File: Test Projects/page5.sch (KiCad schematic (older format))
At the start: 29 parts, among them P10 CONN_01X08, P11 CONN_01X08, P2 CONN_01X07, P3 CONN_01X08, P4 CONN_01X08, P5 CONN_01X08, P6 CONN_01X08, P8 CONN_01X08, P9 CONN_01X08, U10 SF-4052, U11 SF-4052, U12 SF-4052, U13 SF-4052, U14 SF-4052, U15 SF-4052, U16 SF-4052, U17 SF-4052, U8 SF-4052, U9 SF-4052

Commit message: Tested a few layout sections
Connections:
- net OUT1 is gone; now on net KOUT1: U8.13 (X)
- net OUT2 is gone; now on net KOUT2: U8.3 (Y)
- net OUT3 is gone; now on net KOUT3: U9.13 (X)
- net OUT4 is gone; now on net KOUT4: U9.3 (Y)
- net OUT5 is gone; now on net KOUT5: U10.13 (X)
- net OUT6 is gone; now on net KOUT6: U10.3 (Y)
- net OUT7 is gone; now on net KOUT7: U11.13 (X)
- net OUT8 is gone; now on net KOUT8: U11.3 (Y)
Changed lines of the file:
@@
 	5700 2950 5650 2950
 Text GLabel 2550 2350 2    50   Input ~ 0
-OUT1
+KOUT1
 Text GLabel 2550 2750 2    50   Input ~ 0
-OUT2
+KOUT2
 Text GLabel 4850 2350 2    50   Input ~ 0
-OUT3
+KOUT3
 Text GLabel 4850 2750 2    50   Input ~ 0
-OUT4
+KOUT4
 Text GLabel 7150 2350 2    50   Input ~ 0
-OUT5
+KOUT5
 Text GLabel 7150 2750 2    50   Input ~ 0
-OUT6
+KOUT6
 Text GLabel 9450 2750 2    50   Input ~ 0
-OUT8
+KOUT8
 Text GLabel 9450 2350 2    50   Input ~ 0
-OUT7
+KOUT7
 Text GLabel 3050 6050 2    50   Input ~ 0
 KA0

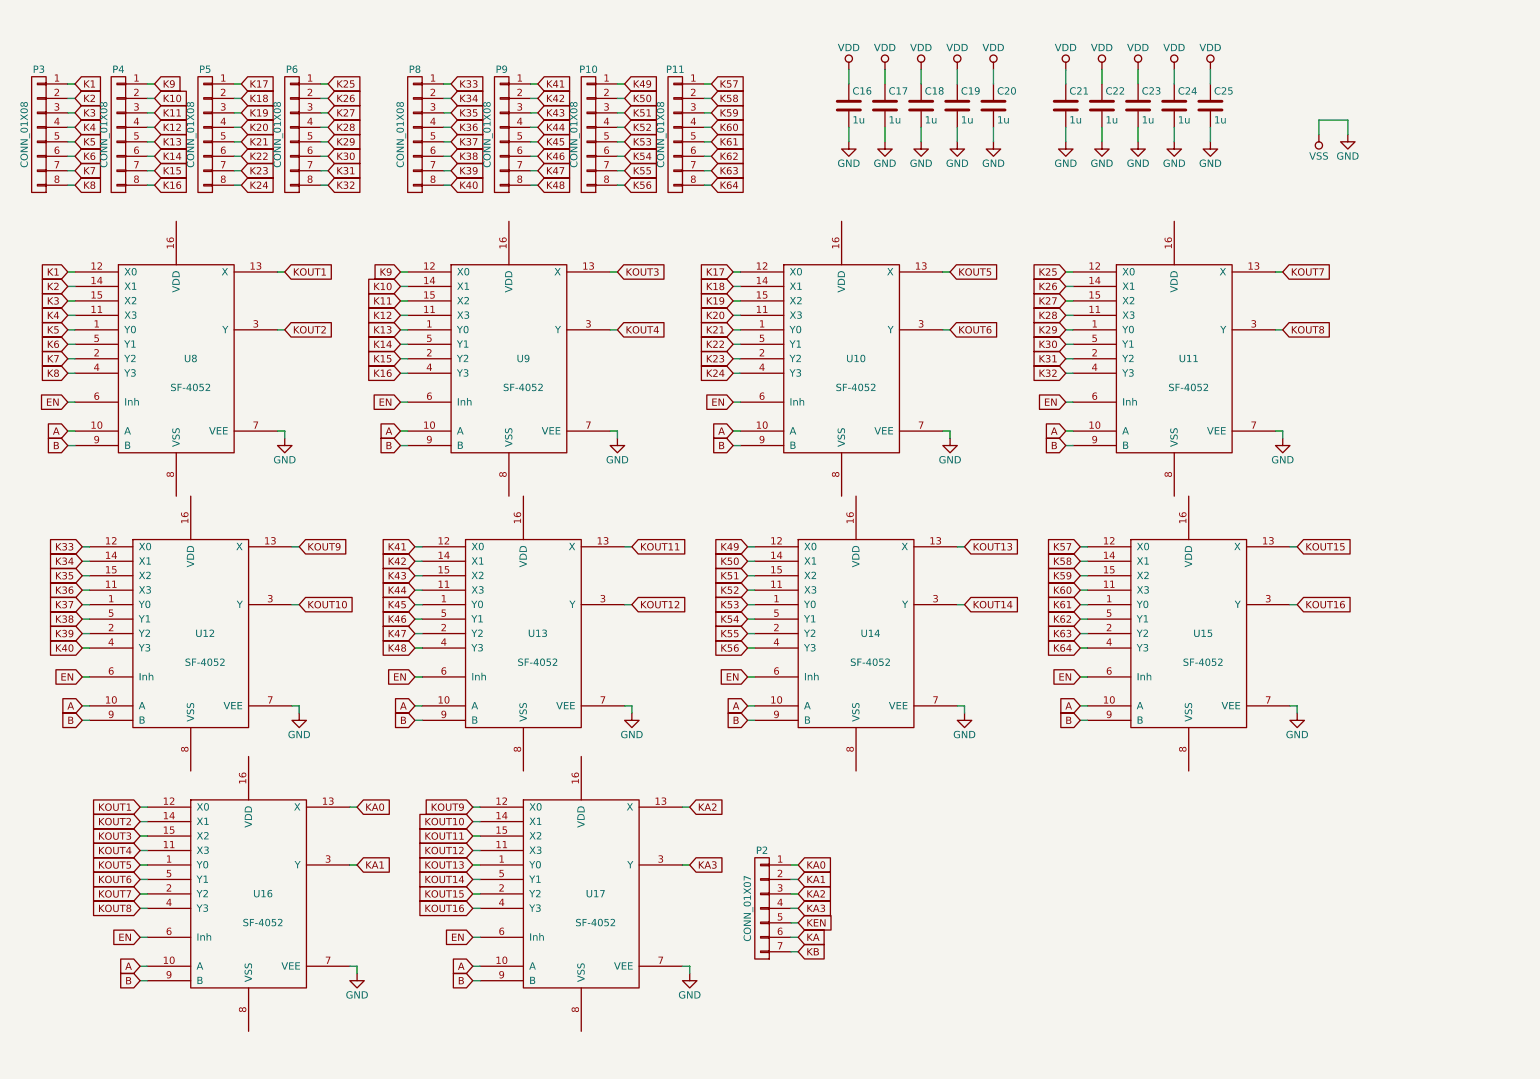
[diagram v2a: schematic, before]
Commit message: Moved to 10x5 size
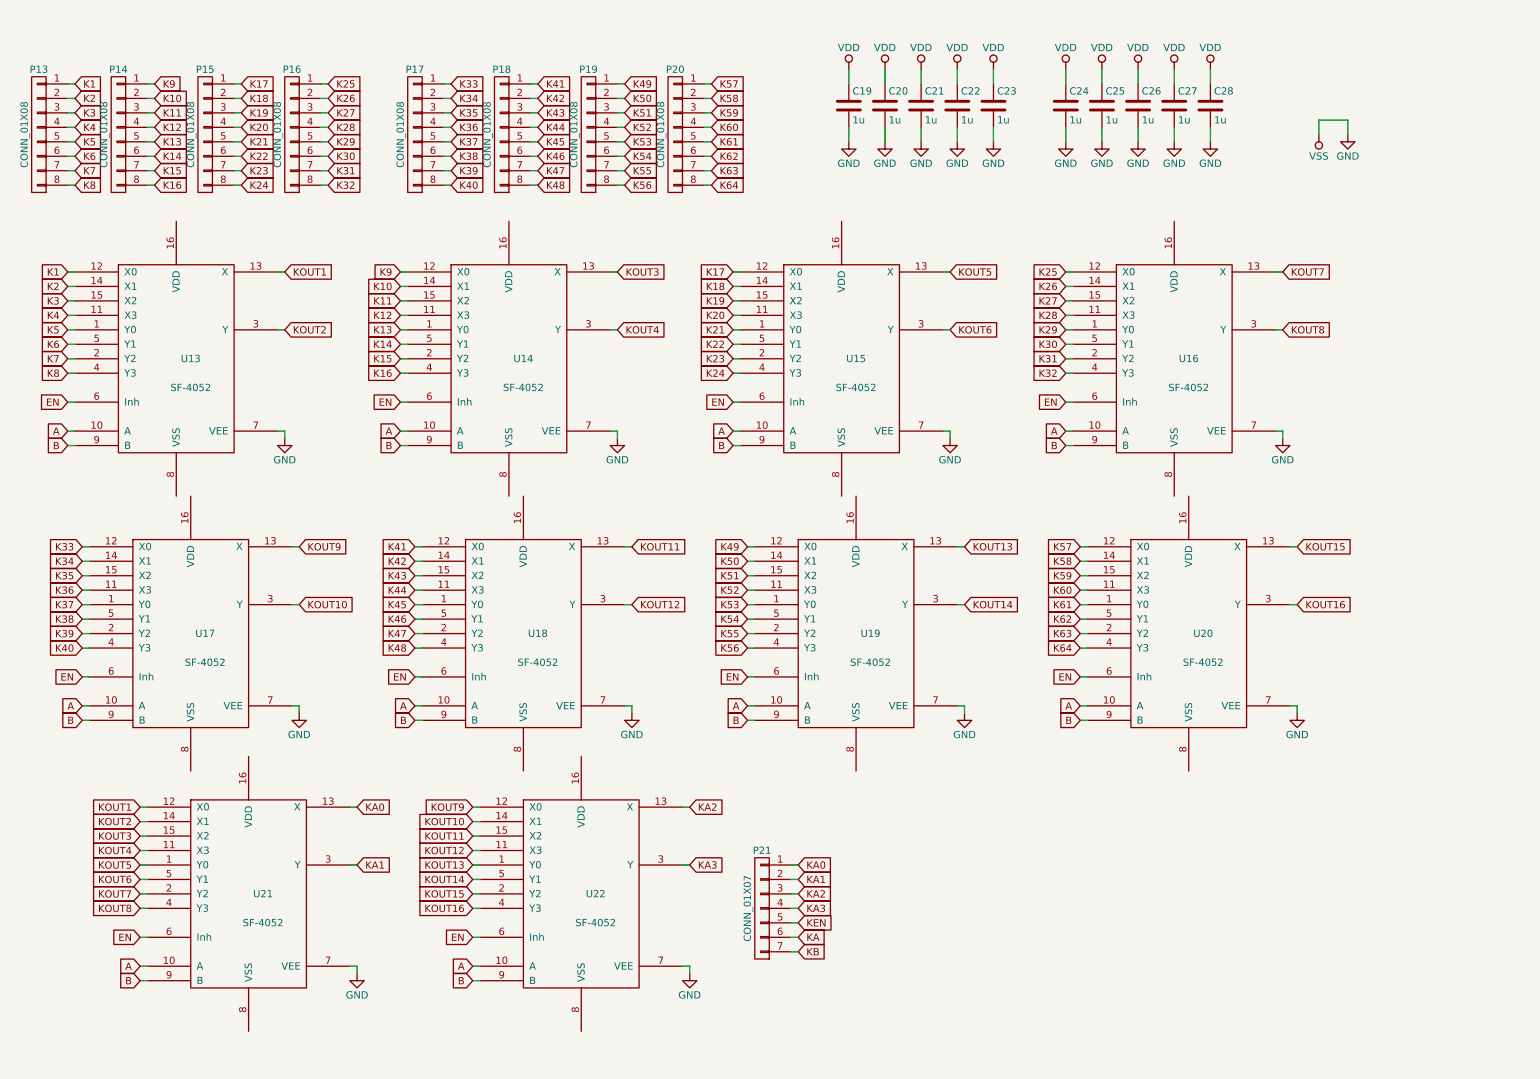
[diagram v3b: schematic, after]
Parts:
- renumbered C16 to C19, C17 to C20, C18 to C21, C19 to C22, C20 to C23, C21 to C24, C22 to C25, C23 to C26, C24 to C27, C25 to C28, P3 to P13, P4 to P14, P5 to P15, P6 to P16, P8 to P17, P9 to P18, P10 to P19, P11 to P20, P2 to P21, U8 to U13, U9 to U14, U10 to U15, U11 to U16, U12 to U17, U13 to U18, U14 to U19, U15 to U20, U16 to U21, U17 to U22
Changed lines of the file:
@@
 $EndDescr
 $Comp
-L C C16
+L C C19
 U 1 1 5688BB67
 P 6450 1200
-F 0 "C16" H 6475 1300 50  0000 L CNN
+F 0 "C19" H 6475 1300 50  0000 L CNN
 F 1 "1u" H 6475 1100 50  0000 L CNN
 F 2 "Capacitors_SMD:C_0603" H 6488 1050 50  0001 C CNN
@@
 	6450 1350 6450 1450
 $Comp
-L C C17
+L C C20
 U 1 1 5688BB6C
 P 6700 1200
-F 0 "C17" H 6725 1300 50  0000 L CNN
+F 0 "C20" H 6725 1300 50  0000 L CNN
 F 1 "1u" H 6725 1100 50  0000 L CNN
 F 2 "Capacitors_SMD:C_0603" H 6738 1050 50  0001 C CNN
@@
 	6700 1350 6700 1450
 $Comp
-L C C18
+L C C21
 U 1 1 5688BB6F
 P 6950 1200
-F 0 "C18" H 6975 1300 50  0000 L CNN
+F 0 "C21" H 6975 1300 50  0000 L CNN
 F 1 "1u" H 6975 1100 50  0000 L CNN
 F 2 "Capacitors_SMD:C_0603" H 6988 1050 50  0001 C CNN
@@
 	6950 1350 6950 1450
 $Comp
-L C C19
+L C C22
 U 1 1 5688BB72
 P 7200 1200
-F 0 "C19" H 7225 1300 50  0000 L CNN
+F 0 "C22" H 7225 1300 50  0000 L CNN
 F 1 "1u" H 7225 1100 50  0000 L CNN
 F 2 "Capacitors_SMD:C_0603" H 7238 1050 50  0001 C CNN
@@
 	7200 1350 7200 1450
 $Comp
-L C C20
+L C C23
 U 1 1 5688BB75
 P 7450 1200
-F 0 "C20" H 7475 1300 50  0000 L CNN
+F 0 "C23" H 7475 1300 50  0000 L CNN
 F 1 "1u" H 7475 1100 50  0000 L CNN
 F 2 "Capacitors_SMD:C_0603" H 7488 1050 50  0001 C CNN
@@
 KB
 $Comp
-L CONN_01X07 P2
+L CONN_01X07 P21
 U 1 1 5688BBDD
 P 5850 6750
-F 0 "P2" H 5850 7150 50  0000 C CNN
+F 0 "P21" H 5850 7150 50  0000 C CNN
 F 1 "CONN_01X07" V 5950 6750 50  0000 C CNN
 F 2 "Pin_Headers:Pin_Header_Straight_1x07" H 5850 6750 50  0001 C CNN
@@
 	6050 7050 6100 7050
 $Comp
-L CONN_01X08 P3
+L CONN_01X08 P13
 U 1 1 5688D7C7
 P 850 1400
-F 0 "P3" H 850 1850 50  0000 C CNN
+F 0 "P13" H 850 1850 50  0000 C CNN
 F 1 "CONN_01X08" V 950 1400 50  0000 C CNN
 F 2 "Pin_Headers:Pin_Header_Straight_1x08" H 850 1400 50  0001 C CNN
@@
 $EndComp
 $Comp
-L CONN_01X08 P4
+L CONN_01X08 P14
 U 1 1 5688ED8C
 P 1400 1400
-F 0 "P4" H 1400 1850 50  0000 C CNN
+F 0 "P14" H 1400 1850 50  0000 C CNN
 F 1 "CONN_01X08" V 1500 1400 50  0000 C CNN
 F 2 "Pin_Headers:Pin_Header_Straight_1x08" H 1400 1400 50  0001 C CNN
@@
 $EndComp
 $Comp
-L CONN_01X08 P5
+L CONN_01X08 P15
 U 1 1 5688EF8A
 P 2000 1400
-F 0 "P5" H 2000 1850 50  0000 C CNN
+F 0 "P15" H 2000 1850 50  0000 C CNN
 F 1 "CONN_01X08" V 2100 1400 50  0000 C CNN
 F 2 "Pin_Headers:Pin_Header_Straight_1x08" H 2000 1400 50  0001 C CNN
@@
 $EndComp
 $Comp
-L CONN_01X08 P6
+L CONN_01X08 P16
 U 1 1 5688F052
 P 2600 1400
-F 0 "P6" H 2600 1850 50  0000 C CNN
+F 0 "P16" H 2600 1850 50  0000 C CNN
 F 1 "CONN_01X08" V 2700 1400 50  0000 C CNN
 F 2 "Pin_Headers:Pin_Header_Straight_1x08" H 2600 1400 50  0001 C CNN
@@
 $EndComp
 $Comp
-L C C21
+L C C24
 U 1 1 568900D7
 P 7950 1200
-F 0 "C21" H 7975 1300 50  0000 L CNN
+F 0 "C24" H 7975 1300 50  0000 L CNN
 F 1 "1u" H 7975 1100 50  0000 L CNN
 F 2 "Capacitors_SMD:C_0603" H 7988 1050 50  0001 C CNN
@@
 	7950 1350 7950 1450
 $Comp
-L C C22
+L C C25
 U 1 1 568900F7
 P 8200 1200
-F 0 "C22" H 8225 1300 50  0000 L CNN
+F 0 "C25" H 8225 1300 50  0000 L CNN
 F 1 "1u" H 8225 1100 50  0000 L CNN
 F 2 "Capacitors_SMD:C_0603" H 8238 1050 50  0001 C CNN
@@
 	8200 1350 8200 1450
 $Comp
-L C C23
+L C C26
 U 1 1 5689010B
 P 8450 1200
-F 0 "C23" H 8475 1300 50  0000 L CNN
+F 0 "C26" H 8475 1300 50  0000 L CNN
 F 1 "1u" H 8475 1100 50  0000 L CNN
 F 2 "Capacitors_SMD:C_0603" H 8488 1050 50  0001 C CNN
@@
 	8450 1350 8450 1450
 $Comp
-L C C24
+L C C27
 U 1 1 5689011F
 P 8700 1200
-F 0 "C24" H 8725 1300 50  0000 L CNN
+F 0 "C27" H 8725 1300 50  0000 L CNN
 F 1 "1u" H 8725 1100 50  0000 L CNN
 F 2 "Capacitors_SMD:C_0603" H 8738 1050 50  0001 C CNN
@@
 	8700 1350 8700 1450
 $Comp
-L C C25
+L C C28
 U 1 1 56890133
 P 8950 1200
-F 0 "C25" H 8975 1300 50  0000 L CNN
+F 0 "C28" H 8975 1300 50  0000 L CNN
 F 1 "1u" H 8975 1100 50  0000 L CNN
 F 2 "Capacitors_SMD:C_0603" H 8988 1050 50  0001 C CNN
@@
 	1150 5150 1200 5150
 $Comp
-L CONN_01X08 P8
+L CONN_01X08 P17
 U 1 1 56890254
 P 3450 1400
-F 0 "P8" H 3450 1850 50  0000 C CNN
+F 0 "P17" H 3450 1850 50  0000 C CNN
 F 1 "CONN_01X08" V 3550 1400 50  0000 C CNN
 F 2 "Pin_Headers:Pin_Header_Straight_1x08" H 3450 1400 50  0001 C CNN
@@
 $EndComp
 $Comp
-L CONN_01X08 P9
+L CONN_01X08 P18
 U 1 1 5689025A
 P 4050 1400
-F 0 "P9" H 4050 1850 50  0000 C CNN
+F 0 "P18" H 4050 1850 50  0000 C CNN
 F 1 "CONN_01X08" V 4150 1400 50  0000 C CNN
 F 2 "Pin_Headers:Pin_Header_Straight_1x08" H 4050 1400 50  0001 C CNN
@@
 $EndComp
 $Comp
-L CONN_01X08 P10
+L CONN_01X08 P19
 U 1 1 56890260
 P 4650 1400
-F 0 "P10" H 4650 1850 50  0000 C CNN
+F 0 "P19" H 4650 1850 50  0000 C CNN
 F 1 "CONN_01X08" V 4750 1400 50  0000 C CNN
 F 2 "Pin_Headers:Pin_Header_Straight_1x08" H 4650 1400 50  0001 C CNN
@@
 $EndComp
 $Comp
-L CONN_01X08 P11
+L CONN_01X08 P20
 U 1 1 56890266
 P 5250 1400
-F 0 "P11" H 5250 1850 50  0000 C CNN
+F 0 "P20" H 5250 1850 50  0000 C CNN
 F 1 "CONN_01X08" V 5350 1400 50  0000 C CNN
 F 2 "Pin_Headers:Pin_Header_Straight_1x08" H 5250 1400 50  0001 C CNN
@@
 	6100 6450 6050 6450
 $Comp
-L SF-4052 U8
+L SF-4052 U13
 U 1 1 5689B3AF
 P 1800 2950
-F 0 "U8" H 1900 2950 50  0000 C CNN
+F 0 "U13" H 1900 2950 50  0000 C CNN
 F 1 "SF-4052" H 1900 2750 50  0000 C CNN
 F 2 "SparkFun-Footprints:SF-SOIC-16" H 1800 2950 60  0001 C CNN
@@
 $EndComp
 $Comp
-L SF-4052 U9
+L SF-4052 U14
 U 1 1 5689B6B5
 P 4100 2950
-F 0 "U9" H 4200 2950 50  0000 C CNN
+F 0 "U14" H 4200 2950 50  0000 C CNN
 F 1 "SF-4052" H 4200 2750 50  0000 C CNN
 F 2 "SparkFun-Footprints:SF-SOIC-16" H 4100 2950 60  0001 C CNN
@@
 $EndComp
 $Comp
-L SF-4052 U10
+L SF-4052 U15
 U 1 1 5689B744
 P 6400 2950
-F 0 "U10" H 6500 2950 50  0000 C CNN
+F 0 "U15" H 6500 2950 50  0000 C CNN
 F 1 "SF-4052" H 6500 2750 50  0000 C CNN
 F 2 "SparkFun-Footprints:SF-SOIC-16" H 6400 2950 60  0001 C CNN
@@
 $EndComp
 $Comp
-L SF-4052 U11
+L SF-4052 U16
 U 1 1 5689B7EE
 P 8700 2950
-F 0 "U11" H 8800 2950 50  0000 C CNN
+F 0 "U16" H 8800 2950 50  0000 C CNN
 F 1 "SF-4052" H 8800 2750 50  0000 C CNN
 F 2 "SparkFun-Footprints:SF-SOIC-16" H 8700 2950 60  0001 C CNN
@@
 $EndComp
 $Comp
-L SF-4052 U12
+L SF-4052 U17
 U 1 1 5689B88B
 P 1900 4850
-F 0 "U12" H 2000 4850 50  0000 C CNN
+F 0 "U17" H 2000 4850 50  0000 C CNN
 F 1 "SF-4052" H 2000 4650 50  0000 C CNN
 F 2 "SparkFun-Footprints:SF-SOIC-16" H 1900 4850 60  0001 C CNN
@@
 $EndComp
 $Comp
-L SF-4052 U13
+L SF-4052 U18
 U 1 1 5689B961
 P 4200 4850
-F 0 "U13" H 4300 4850 50  0000 C CNN
+F 0 "U18" H 4300 4850 50  0000 C CNN
 F 1 "SF-4052" H 4300 4650 50  0000 C CNN
 F 2 "SparkFun-Footprints:SF-SOIC-16" H 4200 4850 60  0001 C CNN
@@
 $EndComp
 $Comp
-L SF-4052 U14
+L SF-4052 U19
 U 1 1 5689BA0E
 P 6500 4850
-F 0 "U14" H 6600 4850 50  0000 C CNN
+F 0 "U19" H 6600 4850 50  0000 C CNN
 F 1 "SF-4052" H 6600 4650 50  0000 C CNN
 F 2 "SparkFun-Footprints:SF-SOIC-16" H 6500 4850 60  0001 C CNN
@@
 $EndComp
 $Comp
-L SF-4052 U15
+L SF-4052 U20
 U 1 1 5689BAC4
 P 8800 4850
-F 0 "U15" H 8900 4850 50  0000 C CNN
+F 0 "U20" H 8900 4850 50  0000 C CNN
 F 1 "SF-4052" H 8900 4650 50  0000 C CNN
 F 2 "SparkFun-Footprints:SF-SOIC-16" H 8800 4850 60  0001 C CNN
@@
 $EndComp
 $Comp
-L SF-4052 U16
+L SF-4052 U21
 U 1 1 5689BB65
 P 2300 6650
-F 0 "U16" H 2400 6650 50  0000 C CNN
+F 0 "U21" H 2400 6650 50  0000 C CNN
 F 1 "SF-4052" H 2400 6450 50  0000 C CNN
 F 2 "SparkFun-Footprints:SF-SOIC-16" H 2300 6650 60  0001 C CNN
@@
 $EndComp
 $Comp
-L SF-4052 U17
+L SF-4052 U22
 U 1 1 5689BC45
 P 4600 6650
-F 0 "U17" H 4700 6650 50  0000 C CNN
+F 0 "U22" H 4700 6650 50  0000 C CNN
 F 1 "SF-4052" H 4700 6450 50  0000 C CNN
 F 2 "SparkFun-Footprints:SF-SOIC-16" H 4600 6650 60  0001 C CNN

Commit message: Post review with Byron
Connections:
- net GND: now also U13.8 (VSS), U14.8 (VSS), U15.8 (VSS), U16.8 (VSS), U17.8 (VSS), U18.8 (VSS), U19.8 (VSS), U20.8 (VSS), U21.8 (VSS), U22.8 (VSS)
- net VDD: now also U13.16 (VDD), U14.16 (VDD), U15.16 (VDD), U16.16 (VDD), U17.16 (VDD), U18.16 (VDD), U19.16 (VDD), U20.16 (VDD), U21.16 (VDD), U22.16 (VDD)
